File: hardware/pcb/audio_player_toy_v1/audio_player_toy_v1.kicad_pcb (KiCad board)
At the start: 2 copper layers, 75 x 60 mm, 19 parts, among them J1 Conn_02x05_Odd_Even, U1 ISD2360YYI, U2 BH-AAA-B5AA005

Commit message: chore: complete finding all footprints, ready to routing, both version
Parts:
- removed the U1 at (156.2, 134.7)
- added C4: 0.1uF, Resistor_SMD:R_0603_1608Metric, F.Cu at (141.4, 79.4)
- added C5: 10uF, Resistor_SMD:R_0603_1608Metric, F.Cu at (141.4, 81.9)
- added U2: ISD2360YYI, .pretty:TQFN-32_L5.0-W5.0-P0.50-BL-EP3.5, F.Cu at (146.8, 81.6)
- C2, C3: value 4.7uF -> 47uF; footprint Capacitor_SMD:C_0603_1608Metric -> .pretty:CASE-A_3216
- moved C1 63.1 mm to (145.3, 73.2), turned to 0 degrees
- moved D1 61.1 mm to (145.6, 86.5), turned to 0 degrees
- moved C3 58.4 mm to (162.8, 82.0), turned to 0 degrees
- moved C2 51.3 mm to (162.8, 79.3)
- moved R1 51.0 mm to (141.4, 84.4), turned to 0 degrees
- moved R2 39.6 mm to (141.4, 86.9)
- moved R3 37.9 mm to (141.4, 89.5)
- moved J1 33.3 mm to (134.6, 70.6), turned to 0 degrees
- renumbered U2 to U1
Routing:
- net BAT+: track 101.5 -> 0.00 mm
- net RDY/BSYB: track 94.4 -> 0.00 mm
- net INTB: track 80.9 -> 0.00 mm, vias 2 -> 0
- net MOSI: track 42.5 -> 0.00 mm, vias 1 -> 0
- net SPK+: track 41.9 -> 0.00 mm, vias 1 -> 0
- net SCLK: track 41.8 -> 0.00 mm, vias 2 -> 0
- net SPK-: track 41.8 -> 0.00 mm, vias 1 -> 0
- net MISO: track 38.1 -> 0.00 mm, vias 2 -> 0
- net SSB: track 32.9 -> 0.00 mm, vias 1 -> 0
- net GPIO5: track 32.3 -> 0.00 mm, vias 1 -> 0
- net GND: track 7.81 -> 0.00 mm, vias 390 -> 0
- net Net-(D1-A): vias 4 -> 0
- removed copper zone on F.Cu, net BAT+
- removed copper zone on F.Cu, net Net-(D1-A)
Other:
- board text added: "${REFERENCE}"

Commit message: feat: complete sch and pcb of v1
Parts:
- removed H1, H2, H3, H4: MountingHole, MountingHole:MountingHole_3.2mm_M3
- removed R1, R2: 10K, Resistor_SMD:R_0603_1608Metric
- removed S1, S2: MX1A-11NN, .pretty:SW_MX1A-11NN
- C1: value EEEFK1A221V -> TAJA226M010RNJ; footprint .pretty:CAP_EEEFK1A221V -> .pretty:CAPMP3216X180N
- moved C3 67.3 mm to (124.0, 137.0), turned to -90 degrees
- moved C1 66.7 mm to (134.6, 139.1), turned to 90 degrees
- moved C2 60.4 mm to (124.0, 125.6), turned to 90 degrees
- moved D1 58.5 mm to (134.6, 144.0), turned to 90 degrees
- moved C5 57.9 mm to (122.3, 136.6), turned to -90 degrees
- moved U2 56.2 mm to (120.0, 130.9), turned to -90 degrees
- moved C4 50.3 mm to (122.3, 125.9), turned to 90 degrees
- moved J1 39.8 mm to (133.5, 110.4)
- moved R3 38.8 mm to (110.9, 113.4), turned to 90 degrees
- moved S3 37.5 mm to (120.0, 115.1)
- moved LS1 31.3 mm to (106.5, 160.0)
- moved LS2 21.0 mm to (120.0, 151.6)
- moved U1 17.8 mm to (120.0, 132.5), turned to -90 degrees
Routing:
- net BAT+: track 0.00 -> 78.2 mm, vias 0 -> 2
- net SPK-: track 0.00 -> 39.4 mm
- net SPK+: track 0.00 -> 39.3 mm
- net MOSI: track 0.00 -> 31.4 mm, vias 0 -> 3
- net RDY/BSYB: track 0.00 -> 31.3 mm, vias 0 -> 2
- net SSB: track 0.00 -> 30.3 mm, vias 0 -> 2
- net INTB: track 0.00 -> 27.9 mm, vias 0 -> 2
- net MISO: track 0.00 -> 27.6 mm, vias 0 -> 2
- net SCLK: track 0.00 -> 23.8 mm, vias 0 -> 2
- net GPIO5: track 0.00 -> 23.6 mm, vias 0 -> 2
- net GND: track 0.00 -> 7.81 mm, vias 0 -> 220
- net Net-(D1-A): vias 0 -> 4
- added copper zone on F.Cu, net BAT+
- added copper zone on F.Cu, net Net-(D1-A)
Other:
- board size 75 x 60 mm -> 40 x 65 mm
- board text added: "audio_player_toy_v1 2026-04-04"
- board text removed: "${REFERENCE}"
- board text removed: "audio_player_toy_v1 2026-04-02"

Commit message: chore: update decoupling caps in v1
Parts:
- C2, C3: value 47uF -> 4.7uF; footprint .pretty:CASE-A_3216 -> Capacitor_SMD:C_0603_1608Metric
- moved C2 0.38 mm to (123.9, 125.9)
- moved C3 0.37 mm to (123.9, 136.6)

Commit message: fix: fix annotation
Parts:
- removed R3: 10K, Resistor_SMD:R_0603_1608Metric
- removed S3: MX1A-11NN, .pretty:SW_MX1A-11NN
- added R1: 10K, Resistor_SMD:R_0603_1608Metric, F.Cu at (110.9, 113.4)
- added S1: MX1A-11NN, .pretty:SW_MX1A-11NN, F.Cu at (120.0, 115.1)
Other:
- board text added: "X RDY INTB SSB MOSI MISO SCLK BAT+ GND GND"
- board text added: "audio_player_toy_v1 2026-04-09"
- board text removed: "audio_player_toy_v1 2026-04-04"

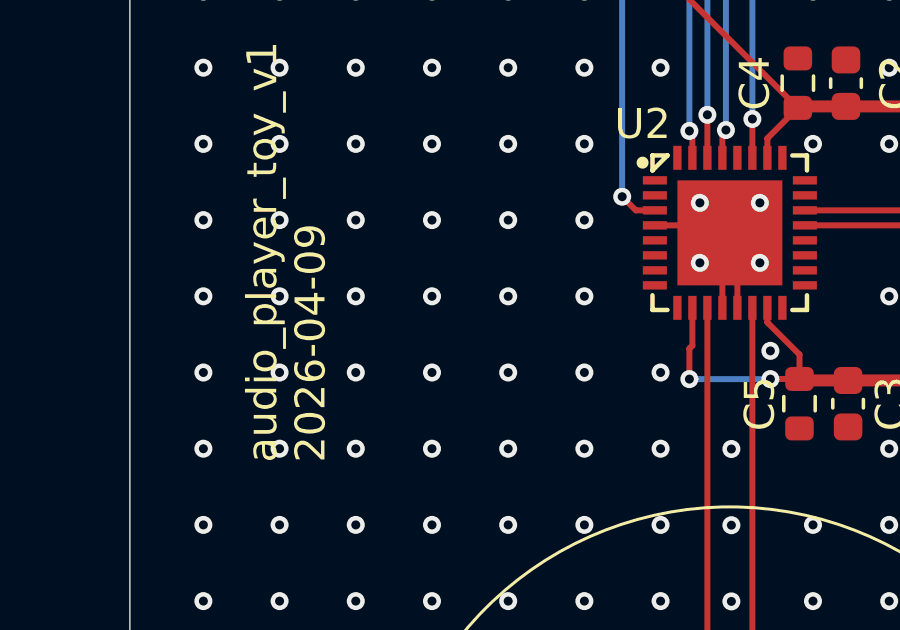
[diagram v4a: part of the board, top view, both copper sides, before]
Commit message: chore: add label on v1 and v2
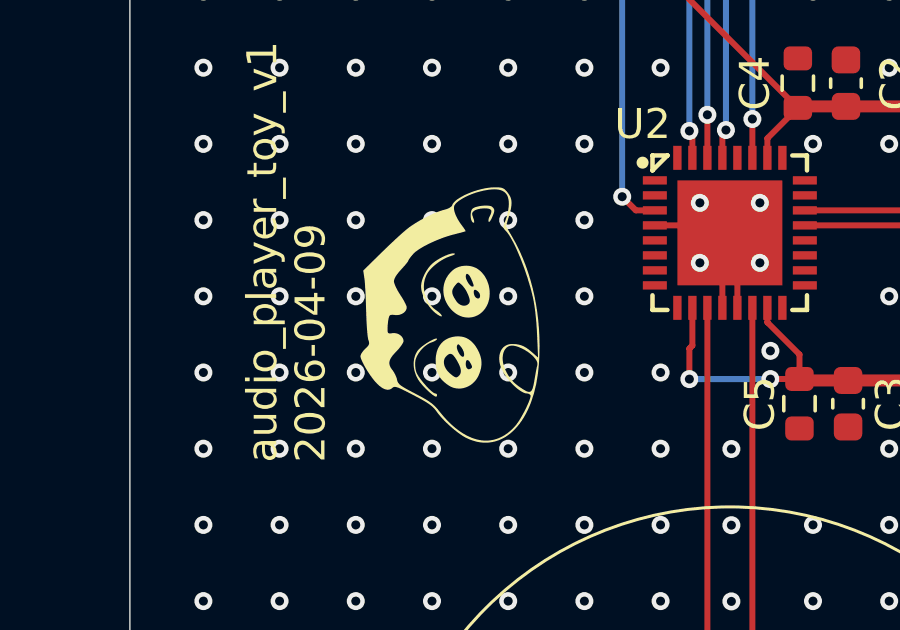
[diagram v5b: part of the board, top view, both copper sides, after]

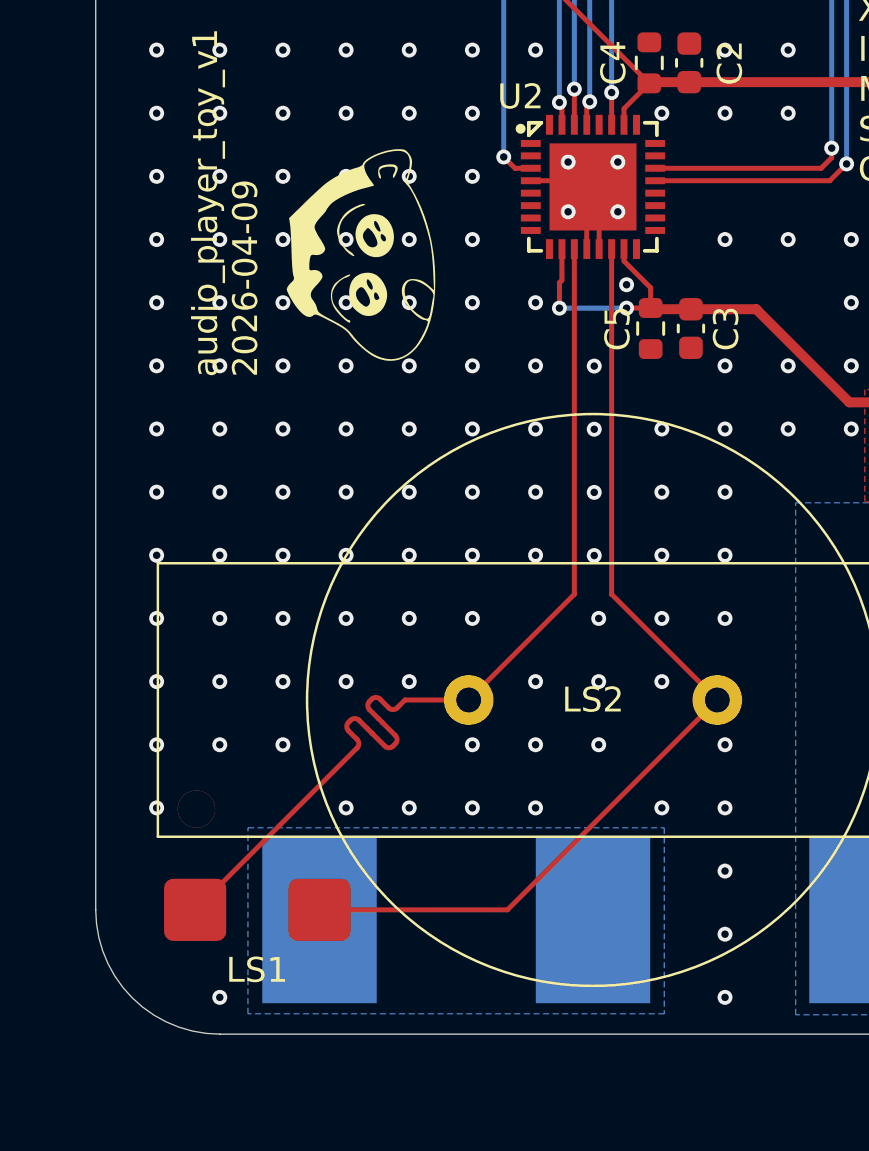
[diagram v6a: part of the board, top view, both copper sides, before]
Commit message: doc: generate all production data
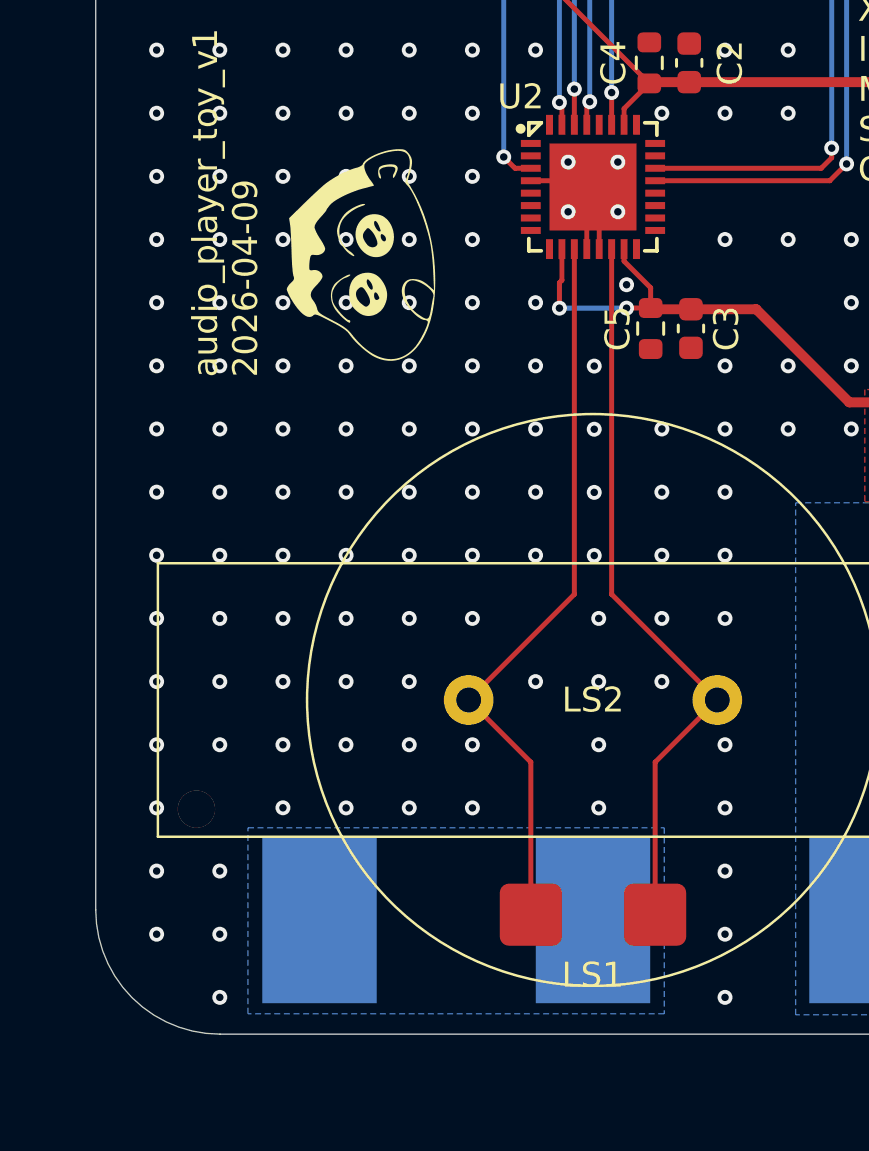
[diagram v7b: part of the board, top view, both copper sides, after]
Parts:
- moved LS1 13.5 mm to (120.0, 160.2)
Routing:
- net SPK-: track 39.4 -> 29.6 mm
- net SPK+: track 39.3 -> 29.6 mm
- net GND: vias 220 -> 225
